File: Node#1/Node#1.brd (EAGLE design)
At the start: 160 x 100 mm, 194 parts, among them J1 1757242, J2 DCJ200-10-A-XX-X_REVA, K1 FTR-K1CK005W, K2 FTR-K1CK005W, K3 FTR-K1CK005W, K4 FTR-K1CK005W, U1 BLUENRG-232, U10 ULN2003AIDG4, U12 ACS723LLCTR-40AB-T, U13 RV8564C3, U14 ACS723LLCTR-40AB-T, U2 SEMTECH_SX1503I091TRTSEMTECH_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, U3 MIC4468YWM, U4 LM339ADR, U5 74HC08D,652, U6 SN74LVC1G74DCUR, U7 TMP75BID, U8 IRM-05-5, U9 LMS8117AMP-3.3, X1 2081-1228, X2 2081-1228, X3 2081-1228, X4 2081-1222, Y1 ECS-160-12-36-AGN-TR, Y2 NX2012SA-32.768K-STD-MUB-1

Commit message: Schematic finished (hopefully) !
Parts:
- removed L1: (no value), rcl:L5650M
- added U$18: LIND, BlueHome:INDM1200X1200X1000N
- U$3, U$4: value L -> L0402
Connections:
- net N$15 renamed IO0
- net N$20 renamed IO3
- net N$21 renamed IO4
- net N$22 renamed IO5
- net N$23 renamed IO9
- net N$25 renamed IO8
- net N$27 renamed IO10
- net N$28 renamed IO11
- net N$29 renamed IO12
- net N$30 renamed IO13
- net N$31 renamed IO14
- net N$32 renamed IO15
- net N$35 renamed IO1
- net N$37 renamed IO2
- net N$47 renamed IO6
- net N$50 renamed IO7
- removed net N$18: R9.1, X1.L7
- removed net N$24: R13.1, X1.L5
- removed net N$26: R24.1, X1.L4
- removed net N$34: R25.1, X1.L3
- removed net N$36: R8.1, X1.L8
- removed net N$40: R12.1, X1.L6
- removed net N$48: JP7.2, R21.1
- removed net N$59: R29.1, X1.L1
- removed net N$61: R28.1, X1.L2
- removed net N$63: JP7.4, R33.1
- removed net N$65: JP7.3, R32.1
- removed net N$68: JP7.6, R37.1
- removed net N$71: JP7.5, R36.1
- new net O_IO0: R8.1, X1.L1
- new net O_IO1: R9.1, X1.L2
- new net O_IO10: R28.1
- new net O_IO11: JP7.2, R29.1, R32.1
- new net O_IO12: JP7.3, R33.1
- new net O_IO13: JP7.4, R36.1
- new net O_IO14: JP7.5, R37.1
- new net O_IO15: JP7.6
- new net O_IO2: R12.1, X1.L3
- new net O_IO3: R13.1, X1.L4
- new net O_IO4: R16.1, X1.L5
- new net O_IO5: R17.1, X1.L6
- new net O_IO6: R20.1, X1.L7
- new net O_IO7: R21.1, X1.L8
- new net O_IO8: R24.1
- new net O_IO9: R25.1
- net E_SHORT: no longer R17.1
- net E_TEMP: no longer R20.1
- net JACK: no longer R16.1
- net N$107: now also U$18.1; no longer L1.1
- net N$116: now also U$18.2; no longer L1.2

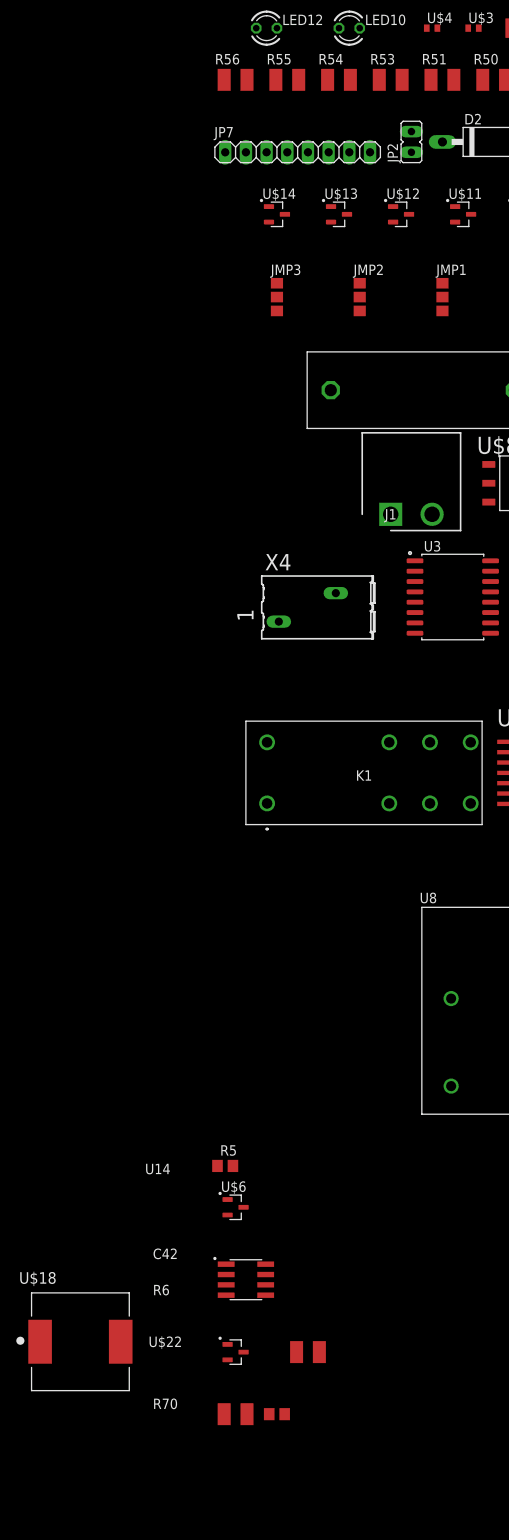
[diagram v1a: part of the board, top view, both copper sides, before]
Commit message: Changed Packages, connected GPIO
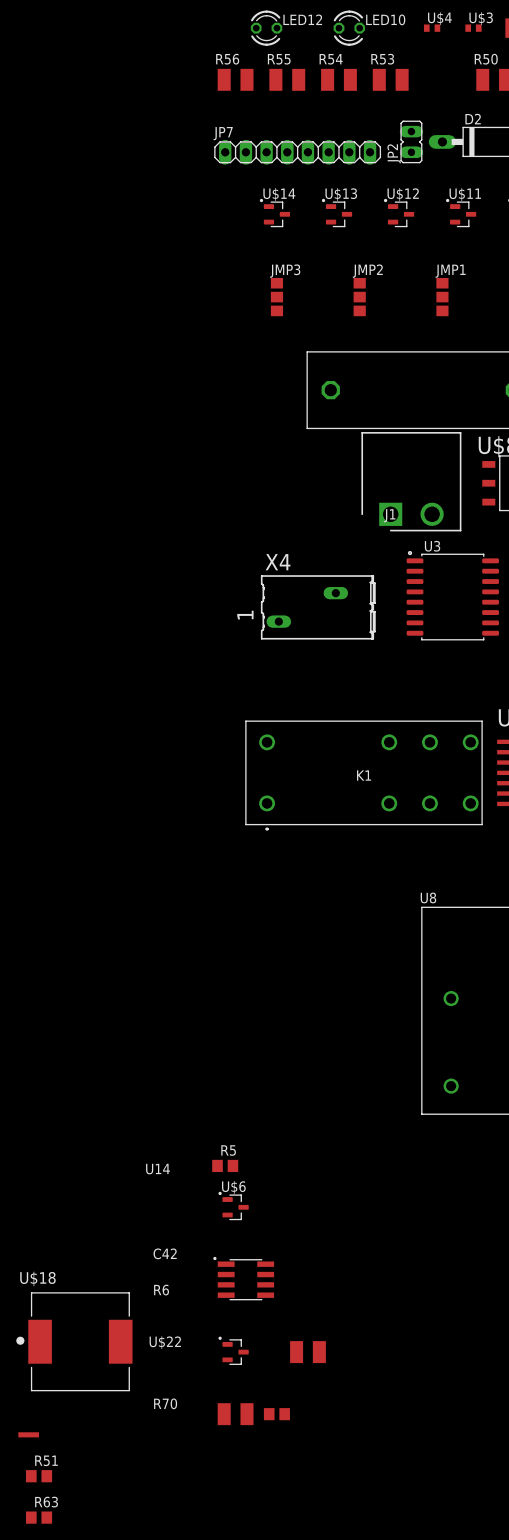
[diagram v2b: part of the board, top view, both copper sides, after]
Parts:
- added R63: (no value), rcl:R0805
- added U$23: STAR_GROUND, BlueHome:STAR_GROUND
- R51: device rcl:R1210 -> rcl:R0805
- moved R51 178.5 mm to (-167.6, -41.9)
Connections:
- new net DIO0: R51.1
- new net DIO1: R63.1
- net AGND: now also U$23.P$1; no longer R51.1
- net GND: now also U$23.P$2; no longer R51.2
- net TDI: now also R51.2
- net TDO: now also R63.2
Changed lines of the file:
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@@
 <attribute name="VALUE" x="-114.3" y="126.365" size="1.27" layer="27"/>
-</element>
-<element name="R51" library="rcl" package="R1210" value="" x="-118.11" y="129.54" smashed="yes">
-<attribute name="NAME" x="-120.65" y="131.445" size="1.27" layer="25"/>
-<attribute name="VALUE" x="-120.65" y="126.365" size="1.27" layer="27"/>
 </element>
 <element name="R52" library="rcl" package="R0805" value="" x="-80.01" y="151.13" smashed="yes">
@@
 <attribute name="NAME" x="-170.103190625" y="-18.2759" size="1.419259375" layer="25"/>
 <attribute name="VALUE" x="-169.978440625" y="-34.358109375" size="1.42205" layer="27"/>
+</element>
+<element name="U$23" library="BlueHome" package="STAR_GROUND" value="STAR_GROUND" x="-168.91" y="-36.83" smashed="yes"/>
+<element name="R51" library="rcl" package="R0805" value="" x="-167.64" y="-41.91" smashed="yes">
+<attribute name="NAME" x="-168.275" y="-40.64" size="1.27" layer="25"/>
+<attribute name="VALUE" x="-168.275" y="-44.45" size="1.27" layer="27"/>
+</element>
+<element name="R63" library="rcl" package="R0805" value="" x="-167.64" y="-46.99" smashed="yes">
+<attribute name="NAME" x="-168.275" y="-45.72" size="1.27" layer="25"/>
+<attribute name="VALUE" x="-168.275" y="-49.53" size="1.27" layer="27"/>
 </element>
 </elements>
@@
 <contactref element="U1" pad="12"/>
 <contactref element="JP1" pad="8"/>
-<wire x1="-83.82" y1="113.03" x2="-48.51" y2="111.865" width="0" layer="19" extent="1-1"/>
+<contactref element="R51" pad="2"/>
+<wire x1="-83.82" y1="113.03" x2="-166.69" y2="-41.91" width="0" layer="19" extent="1-1"/>
+<wire x1="-48.51" y1="111.865" x2="-83.82" y2="113.03" width="0" layer="19" extent="1-1"/>
 </signal>
 <signal name="TDO">
 <contactref element="U1" pad="11"/>
 <contactref element="JP1" pad="6"/>
-<wire x1="-86.36" y1="113.03" x2="-49.01" y2="111.865" width="0" layer="19" extent="1-1"/>
+<contactref element="R63" pad="2"/>
+<wire x1="-86.36" y1="113.03" x2="-166.69" y2="-46.99" width="0" layer="19" extent="1-1"/>
+<wire x1="-49.01" y1="111.865" x2="-86.36" y2="113.03" width="0" layer="19" extent="1-1"/>
 </signal>
 <signal name="N$3">
@@
 <contactref element="C30" pad="2"/>
 <contactref element="R67" pad="1"/>
-<contactref element="R51" pad="2"/>
 <contactref element="U8" pad="VNEG"/>
 <contactref element="U9" pad="1"/>
@@
 <contactref element="R70" pad="1"/>
 <contactref element="U$22" pad="3"/>
+<contactref element="U$23" pad="P$2"/>
+<wire x1="-144.91" y1="-34.29" x2="-169.545" y2="-36.83" width="0" layer="19" extent="1-1"/>
 <wire x1="-139.38" y1="-34.29" x2="-144.91" y2="-34.29" width="0" layer="19" extent="1-1"/>
 <wire x1="-142.53" y1="-26.67" x2="-144.91" y2="-34.29" width="0" layer="19" extent="1-1"/>
@@
 <wire x1="-121.92" y1="142.24" x2="-121.6" y2="151.13" width="0" layer="19" extent="1-1"/>
 <wire x1="-118.73" y1="135.89" x2="-121.92" y2="142.24" width="0" layer="19" extent="1-1"/>
-<wire x1="-116.71" y1="129.54" x2="-118.73" y2="135.89" width="0" layer="19" extent="1-1"/>
 <wire x1="-128.27" y1="135.89" x2="-121.92" y2="142.24" width="0" layer="19" extent="1-1"/>
 <wire x1="-132.08" y1="142.24" x2="-128.27" y2="135.89" width="0" layer="19" extent="1-1"/>
@@
 </signal>
 <signal name="AGND">
-<contactref element="R51" pad="1"/>
 <contactref element="J2" pad="2"/>
 <contactref element="X4" pad="L2"/>
@@
 <contactref element="VR1" pad="A"/>
 <contactref element="VR1" pad="B"/>
-<wire x1="-49.85" y1="156.21" x2="-16.19" y2="156.21" width="0" layer="19" extent="1-1"/>
-<wire x1="-54.93" y1="156.21" x2="-49.85" y2="156.21" width="0" layer="19" extent="1-1"/>
-<wire x1="-92.84" y1="135.89" x2="-54.93" y2="156.21" width="0" layer="19" extent="1-1"/>
-<wire x1="-105.41" y1="121.92" x2="-92.84" y2="135.89" width="0" layer="19" extent="1-1"/>
-<wire x1="-119.51" y1="129.54" x2="-105.41" y2="121.92" width="0" layer="19" extent="1-1"/>
-<wire x1="-92.775" y1="94.615" x2="-105.41" y2="121.92" width="0" layer="19" extent="1-1"/>
-<wire x1="-92.775" y1="92.075" x2="-92.775" y2="94.615" width="0" layer="19" extent="1-1"/>
+<contactref element="U$23" pad="P$1"/>
+<wire x1="-131.2" y1="66.52" x2="-168.275" y2="-36.83" width="0" layer="19" extent="1-1"/>
+<wire x1="-121.48" y1="62.865" x2="-131.2" y2="66.52" width="0" layer="19" extent="1-1"/>
+<wire x1="-112.4204" y1="77.6986" x2="-121.48" y2="62.865" width="0" layer="19" extent="1-1"/>
+<wire x1="-93.3704" y1="77.6986" x2="-112.4204" y2="77.6986" width="0" layer="19" extent="1-1"/>
+<wire x1="-92.775" y1="92.075" x2="-93.3704" y2="77.6986" width="0" layer="19" extent="1-1"/>
+<wire x1="-92.775" y1="94.615" x2="-92.775" y2="92.075" width="0" layer="19" extent="1-1"/>
 <wire x1="-95.25" y1="92.71" x2="-92.775" y2="92.075" width="0" layer="19" extent="1-1"/>
 <wire x1="-87.97" y1="92.71" x2="-92.775" y2="92.075" width="0" layer="19" extent="1-1"/>
-<wire x1="-93.3704" y1="77.6986" x2="-92.775" y2="92.075" width="0" layer="19" extent="1-1"/>
-<wire x1="-112.4204" y1="77.6986" x2="-93.3704" y2="77.6986" width="0" layer="19" extent="1-1"/>
-<wire x1="-121.48" y1="62.865" x2="-112.4204" y2="77.6986" width="0" layer="19" extent="1-1"/>
-<wire x1="-131.2" y1="66.52" x2="-121.48" y2="62.865" width="0" layer="19" extent="1-1"/>
 <wire x1="-74.3204" y1="77.6986" x2="-93.3704" y2="77.6986" width="0" layer="19" extent="1-1"/>
 <wire x1="-55.2704" y1="77.6986" x2="-74.3204" y2="77.6986" width="0" layer="19" extent="1-1"/>
 <wire x1="-56.61" y1="104.14" x2="-55.2704" y2="77.6986" width="0" layer="19" extent="1-1"/>
 <wire x1="-52.61" y1="105.29" x2="-56.61" y2="104.14" width="0" layer="19" extent="1-1"/>
-<wire x1="-141.92" y1="151.13" x2="-119.51" y2="129.54" width="0" layer="19" extent="1-1"/>
+<wire x1="-105.41" y1="121.92" x2="-92.775" y2="94.615" width="0" layer="19" extent="1-1"/>
+<wire x1="-92.84" y1="135.89" x2="-105.41" y2="121.92" width="0" layer="19" extent="1-1"/>
 <wire x1="-44.45" y1="47.89" x2="-55.2704" y2="77.6986" width="0" layer="19" extent="1-1"/>
 <wire x1="-69.5706" y1="44.45" x2="-44.45" y2="47.89" width="0" layer="19" extent="1-1"/>
@@
 <wire x1="-69.5706" y1="41.91" x2="-69.5706" y2="43.18" width="0" layer="19" extent="1-1"/>
 <wire x1="-69.5706" y1="40.64" x2="-69.5706" y2="41.91" width="0" layer="19" extent="1-1"/>
+<wire x1="-54.93" y1="156.21" x2="-92.84" y2="135.89" width="0" layer="19" extent="1-1"/>
+<wire x1="-49.85" y1="156.21" x2="-54.93" y2="156.21" width="0" layer="19" extent="1-1"/>
+<wire x1="-16.19" y1="156.21" x2="-49.85" y2="156.21" width="0" layer="19" extent="1-1"/>
+<wire x1="-141.92" y1="151.13" x2="-105.41" y2="121.92" width="0" layer="19" extent="1-1"/>
 </signal>
 <signal name="N$95">
@@
 <contactref element="JP7" pad="6"/>
 </signal>
+<signal name="DIO0">
+<contactref element="R51" pad="1"/>
+</signal>
+<signal name="DIO1">
+<contactref element="R63" pad="1"/>
+</signal>
 </signals>

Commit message: Created BlueNRG Design Block and Board Size for Node#1
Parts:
- removed ANT1: CONUFL001-SMD, BlueHome:CONUFL001-SMD
- removed C1, C10, C2, C3, C4, C5, C6, C7, C8, C9: (no value), rcl:C0805K
- removed C11, C12, C13, C14, C15, C30: (no value), rcl:C0805
- removed C16, C17: (no value), rcl:C0402
- removed D1: BAS40-06, diode:SOT23
- removed JMP1: 0R-JUMPA, jump-0r-smd:A0R-JMP
- removed JP1: (no value), pinhead:2X05
- removed JP2: (no value), jumper:JP1
- removed JP4: (no value), pinhead:1X03
- removed JP6: (no value), pinhead:1X02
- removed R1, R2, R3, R4, R51, R63: (no value), rcl:R0805
- removed R66, R67: (no value), rcl:R1210
- removed S1, S2: FSM4JSMAATR, BlueHome:SW_FSM4JSMAATR
- removed U$3, U$4: L0402, BlueHome:R0402
- removed U$5: BALF-NRG-01D3, BlueHome:FLIPCHIP
- removed U1: BLUENRG-232, BlueHome:QFN50P500X500X100-33T345N
- removed Y1: ECS-160-12-36-AGN-TR, BlueHome:XTAL_ECS-160-12-36-AGN-TR
- removed Y2: NX2012SA-32.768K-STD-MUB-1, BlueHome:XTAL_NX2012SA-32.768K-STD-MUB-1
- added ANT2: CONUFL001-SMD, BlueHome:CONUFL001-SMD
- added C28, C43, C44, C45, C46, C47, C48, C49, C50, C51: (no value), rcl:C0805K
- added C52, C53, C54, C55, C56, C57: (no value), rcl:C0805
- added C58, C59: (no value), rcl:C0402
- added D4: BAS40-06, diode:SOT23
- added JMP7: 0R-JUMPA, jump-0r-smd:A0R-JMP
- added JP10: (no value), jumper:JP1
- added JP11: (no value), pinhead:1X03
- added JP12: (no value), pinhead:1X02
- added JP9: (no value), pinhead:2X05
- added R64, R71, R72, R73, R76, R77: (no value), rcl:R0805
- added R74, R75: (no value), rcl:R1210
- added S3, S4: FSM4JSMAATR, BlueHome:SW_FSM4JSMAATR
- added U$24, U$26: L0402, BlueHome:R0402
- added U$25: BALF-NRG-01D3, BlueHome:FLIPCHIP
- added U11: BLUENRG-232, BlueHome:QFN50P500X500X100-33T345N
- added Y3: ECS-160-12-36-AGN-TR, BlueHome:XTAL_ECS-160-12-36-AGN-TR
- added Y4: NX2012SA-32.768K-STD-MUB-1, BlueHome:XTAL_NX2012SA-32.768K-STD-MUB-1
- moved K1 234.7 mm to (86.4, 97.8), turned to 270 degrees
- moved U8 148.0 mm to (49.5, 29.2), turned to 270 degrees
- moved K3 141.6 mm to (64.8, 88.9), turned to 180 degrees
- moved K4 139.0 mm to (29.2, 36.8), turned to 270 degrees
- moved K2 120.7 mm to (48.3, 144.8), turned to 270 degrees
- moved X2 101.1 mm to (11.4, 102.9), turned to 90 degrees
- moved X3 94.0 mm to (26.7, -8.89), turned to 270 degrees
- moved X1 15.9 mm to (-8.89, 25.4), turned to 180 degrees
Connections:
- removed net 0V: C12.2, C13.1
- removed net N$1: C7.1, C8.1, U1.28
- removed net N$10: C14.1, U1.23, Y2.2
- removed net N$11: C15.1, U1.22, Y2.1
- removed net N$114: JP6.2, R67.2, S2.3, S2.4
- removed net N$14: U$5.B2, U1.20
- removed net N$16: C17.1, U$3.1, U$5.A1
- removed net N$17: ANT1.1, C16.1, U$3.2
- removed net N$2: C10.1, C9.1, JMP1.2, U1.26
- removed net N$3: JP1.1, JP2.1
- removed net N$4: C12.1, U1.17, Y1.3
- removed net N$5: R2.1, S1.1, S1.2
- removed net N$6: C13.2, U1.18, Y1.1
- removed net N$7: U$5.B1, U1.21
- removed net N$9: C14.2, C15.2, U$4.1
- new net N$15: C48.1, C49.1, U11.28
- new net N$18: C50.1, C51.1, JMP7.2, U11.26
- new net N$20: R71.1, S3.1, S3.2
- new net N$21: C53.1, U11.17, Y3.3
- new net N$22: C54.2, U11.18, Y3.1
- new net N$23: C55.2, C56.2, U$24.1
- new net N$24: C55.1, U11.23, Y4.2
- new net N$25: C56.1, U11.22, Y4.1
- new net N$26: C58.1, U$25.A1, U$26.1
- new net N$27: ANT2.1, C59.1, U$26.2
- new net N$28: JP10.1, JP9.1
- new net N$29: JP12.2, R75.2, S4.3, S4.4
- new net N$30: U$25.B1, U11.20
- new net N$31: U$25.B2, U11.21
- net +3V3: now also C28.1, C43.1, C44.1, C45.1, C46.1, C47.1, D4.2, JMP7.3, JP10.2, R64.2, R72.2, R73.2, R74.2, U11.19, U11.24, U11.6; no longer C1.1, C2.1, C3.1, C4.1, C5.1, C6.1, D1.2, JMP1.3, JP2.2, R1.2, R3.2, R4.2, R66.2, U1.19, U1.24, U1.6
- net ADC1: now also U11.15; no longer U1.15
- net ADC2: now also U11.16; no longer U1.16
- net DIO0: now also R76.1; no longer R51.1
- net DIO1: now also R77.1; no longer R63.1
- net DIO12: now also U11.30; no longer U1.30
- net DIO13: now also U11.29; no longer U1.29
- net DIO14: now also C57.1, JP12.1, R74.1, S4.1, S4.2, U11.13; no longer C30.1, JP6.1, R66.1, S2.1, S2.2, U1.13
- net DIO2: now also U11.10; no longer U1.10
- net DIO3: now also U11.9; no longer U1.9
- net DIO6: now also U11.5; no longer U1.5
- net DIO7: now also U11.4; no longer U1.4
- net GND: now also ANT2.2, ANT2.3, C28.2, C43.2, C44.2, C45.2, C46.2, C47.2, C48.2, C49.2, C50.2, C51.2, C52.1, C53.2, C54.1, C57.2, C58.2, C59.2, JP11.3, JP9.3, JP9.5, JP9.9, R71.2, R75.1, U$24.2, U$25.A2, U11.31, U11.33, Y3.2, Y3.4; no longer ANT1.2, ANT1.3, C1.2, C10.2, C11.1, C16.2, C17.2, C2.2, C3.2, C30.2, C4.2, C5.2, C6.2, C7.2, C8.2, C9.2, JP1.3, JP1.5, JP1.9, JP4.3, R2.2, R67.1, U$4.2, U$5.A2, U1.31, U1.33, Y1.2, Y1.4
- net JTCK: now also JP9.4, U11.2; no longer JP1.4, U1.2
- net JTMS: now also JP9.2, U11.1; no longer JP1.2, U1.1
- net RESETN: now also C52.2, D4.3, JP9.10, R64.1, S3.3, S3.4, U11.25; no longer C11.2, D1.3, JP1.10, R1.1, S1.3, S1.4, U1.25
- net RXD: now also JP11.2, U11.32; no longer JP4.2, U1.32
- net SCL: now also R72.1, U11.8; no longer R3.1, U1.8
- net SDA: now also R73.1, U11.7; no longer R4.1, U1.7
- net SMPSFILT2: now also JMP7.1, U11.27; no longer JMP1.1, U1.27
- net TDI: now also JP9.8, R76.2, U11.12; no longer JP1.8, R51.2, U1.12
- net TDO: now also JP9.6, R77.2, U11.11; no longer JP1.6, R63.2, U1.11
- net TXD: now also JP11.1, U11.3; no longer JP4.1, U1.3
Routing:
- net +3V3: track 0.00 -> 97.6 mm, vias 0 -> 5
- net RESETN: track 0.00 -> 62.0 mm, vias 0 -> 3
- net DIO14: track 0.00 -> 26.7 mm
- net TDI: track 0.00 -> 20.9 mm
- net JTCK: track 0.00 -> 17.5 mm
- net TDO: track 0.00 -> 16.7 mm
- net N$29: track 0.00 -> 14.7 mm
- net SMPSFILT2: track 0.00 -> 14.6 mm
- net JTMS: track 0.00 -> 14.2 mm
- net N$18: track 0.00 -> 14.0 mm
- net N$22: track 0.00 -> 11.7 mm
- net N$21: track 0.00 -> 11.1 mm
- net N$20: track 0.00 -> 11.0 mm
- net RXD: track 0.00 -> 8.51 mm
- net N$25: track 0.00 -> 7.13 mm
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- added copper zone on layer 16, net GND
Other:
- board size 160 x 100 mm -> 62 x 71 mm

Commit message: Added lager Board Layout in Node#1
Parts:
- moved U$18 255.0 mm to (65.4, 88.9), turned to 180 degrees
- moved R53 212.6 mm to (74.9, 55.9), flipped to the bottom, turned to 270 degrees
- moved C22 212.0 mm to (54.6, 48.3), flipped to the bottom, turned to 180 degrees
- moved X4 211.5 mm to (78.1, 66.7), turned to 180 degrees
- moved C23 207.6 mm to (50.8, 60.3), flipped to the bottom
- moved U$6 196.3 mm to (37.6, 66.8), flipped to the bottom, turned to 180 degrees
- moved R5 194.9 mm to (38.4, 62.7)
- moved D2 194.0 mm to (66.7, 45.7), turned to 90 degrees
- moved J1 186.6 mm to (43.2, -5.71), turned to 180 degrees
- moved C24 175.7 mm to (54.6, 50.8), flipped to the bottom, turned to 180 degrees
- moved C25 173.0 mm to (50.2, 62.9), flipped to the bottom
- moved JP8 172.6 mm to (66.7, 59.1)
- moved U$9 169.1 mm to (36.2, 5.08), turned to 180 degrees
- moved C38 166.9 mm to (70.5, 29.2), turned to 270 degrees
- moved R69 165.9 mm to (64.8, 80.0), turned to 270 degrees
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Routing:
- net AGND: track 0.00 -> 80.6 mm, vias 0 -> 1
- net +5V: track 0.00 -> 69.0 mm
- net +3V3: track 97.6 -> 162.3 mm, vias 5 -> 6
- net V+: track 0.00 -> 46.8 mm
- net RELAY4: track 0.00 -> 41.9 mm
- net N$42: track 0.00 -> 39.9 mm
- net N$116: track 0.00 -> 39.1 mm, vias 0 -> 1
- net RELAY3: track 0.00 -> 33.4 mm
- net N$98: track 0.00 -> 22.8 mm, vias 0 -> 1
- net N$45: track 0.00 -> 15.5 mm
- net N$107: track 0.00 -> 15.2 mm
- net RELAY2: track 0.00 -> 14.2 mm
- net L2: track 0.00 -> 14.2 mm
- net +3V3_RTC: track 0.00 -> 14.1 mm
- net CURR_SENS_RELAY: track 0.00 -> 12.9 mm
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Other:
- board size 62 x 71 mm -> 260 x 170 mm
- board text added: "hoch 71 breit 62"

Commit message: Worked on Layout for Node#1
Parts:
- added X5: (no value), con-wago-500:W237-102
- R39, R40, R41, R42, R43, R44, R45, R46, R47, R48, R49, R50, R58, R59, R6, R60, R61, R70, R74, R75: device rcl:R1210 -> rcl:M0805
- R52: device rcl:R0805 -> rcl:M0805
- moved U$23 228.4 mm to (39.9, 55.9)
- moved R56 166.8 mm to (-15.5, 22.6), turned to 270 degrees
- moved R54 145.8 mm to (-31.5, 22.9), turned to 270 degrees
- moved R65 141.6 mm to (30.7, 32.5), flipped to the bottom, turned to 180 degrees
- moved R55 139.4 mm to (-47.5, 22.9), turned to 270 degrees
- moved U3 126.8 mm to (6.86, 38.1), flipped to the bottom
- moved U$19 126.2 mm to (35.3, 29.7), flipped to the bottom, turned to 180 degrees
- moved R70 125.3 mm to (-46.2, 44.7), turned to 270 degrees
- moved C42 124.7 mm to (-40.8, 43.2)
- moved U14 120.3 mm to (-41.4, 47.8), turned to 270 degrees
- moved U$22 119.2 mm to (-46.7, 42.9), flipped to the bottom, turned to 90 degrees
- moved R62 116.5 mm to (30.7, 29.3), flipped to the bottom, turned to 180 degrees
- moved R42 114.1 mm to (-6.10, 29.5), turned to 180 degrees
- moved R45 113.8 mm to (-14.7, 36.3), flipped to the bottom
- moved R46 111.9 mm to (-25.1, 35.8), flipped to the bottom
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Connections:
- net L1: now also X3.L8, X5.2; no longer X3.L1
- net L2: now also X3.L7, X5.1; no longer X3.L2
- net L3: now also X3.L6; no longer X3.L3
- net L4: now also X3.L5; no longer X3.L4
- net L5: now also X3.L4; no longer X3.L5
- net L6: now also X3.L3; no longer X3.L6
- net L7: now also X3.L2; no longer X3.L7
- net L8: now also X3.L1; no longer X3.L8
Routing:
- net +5V: track 69.0 -> 274.2 mm, vias 0 -> 1
- net V+: track 46.8 -> 206.5 mm, vias 0 -> 2
- net ADC2: track 2.74 -> 130.4 mm, vias 1 -> 4
- net SCL: track 4.98 -> 110.1 mm, vias 1 -> 6
- net SDA: track 5.71 -> 107.2 mm, vias 1 -> 4
- net L1: track 7.50 -> 107.5 mm, vias 0 -> 2
- net CURR_SENS_PWM: track 0.00 -> 84.1 mm
- net N$53: track 0.00 -> 69.5 mm, vias 0 -> 3
- net DIO12: track 2.25 -> 69.9 mm, vias 1 -> 4
- net DIO13: track 1.81 -> 60.4 mm, vias 1 -> 8
- net N$67: track 0.00 -> 56.9 mm, vias 0 -> 3
- net L7: track 0.00 -> 52.9 mm, vias 0 -> 2
- net L5: track 0.00 -> 49.6 mm, vias 0 -> 2
- net L3: track 0.00 -> 47.9 mm, vias 0 -> 2
- net L2: track 14.2 -> 61.1 mm, vias 0 -> 1
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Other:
- outline, holes or cut-outs redrawn
- board text added: "STECKER GRÖßE??"
